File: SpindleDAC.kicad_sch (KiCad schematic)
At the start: 18 parts, among them J25 Spindle Out, Q1 BC847, U17 LTV-247, U18 TL431A

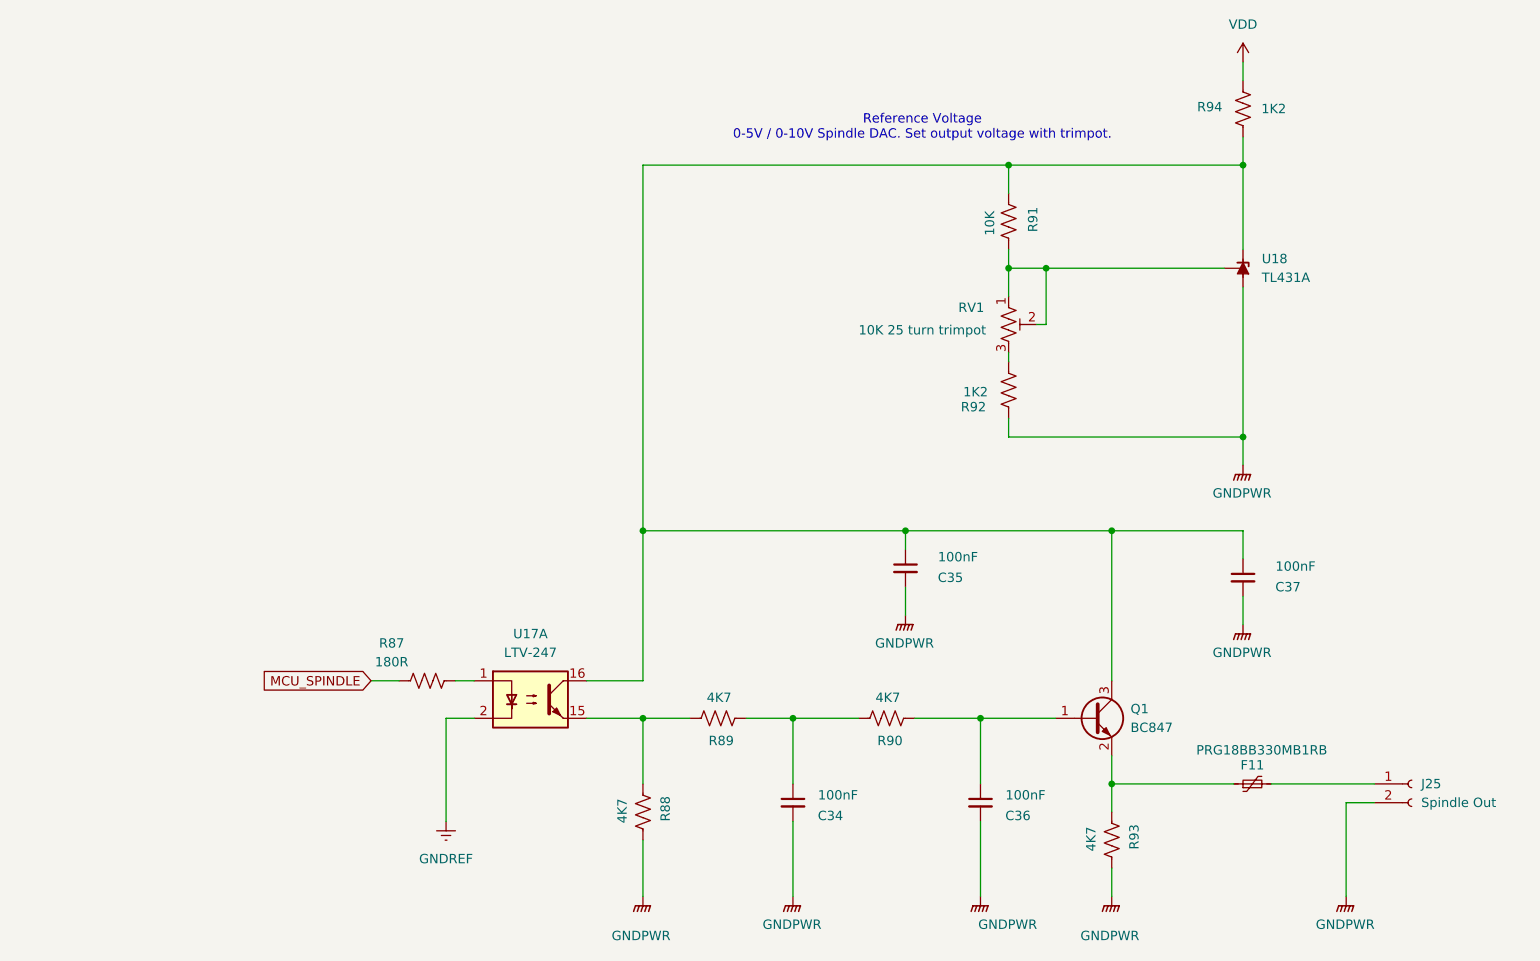
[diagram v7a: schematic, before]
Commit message: Switched terminal footprints over to a finer pitch. Corrected an issue with component reference values preventing proper use of multi channel rule areas. Component references for 4 channel optos are more straightforward as a result
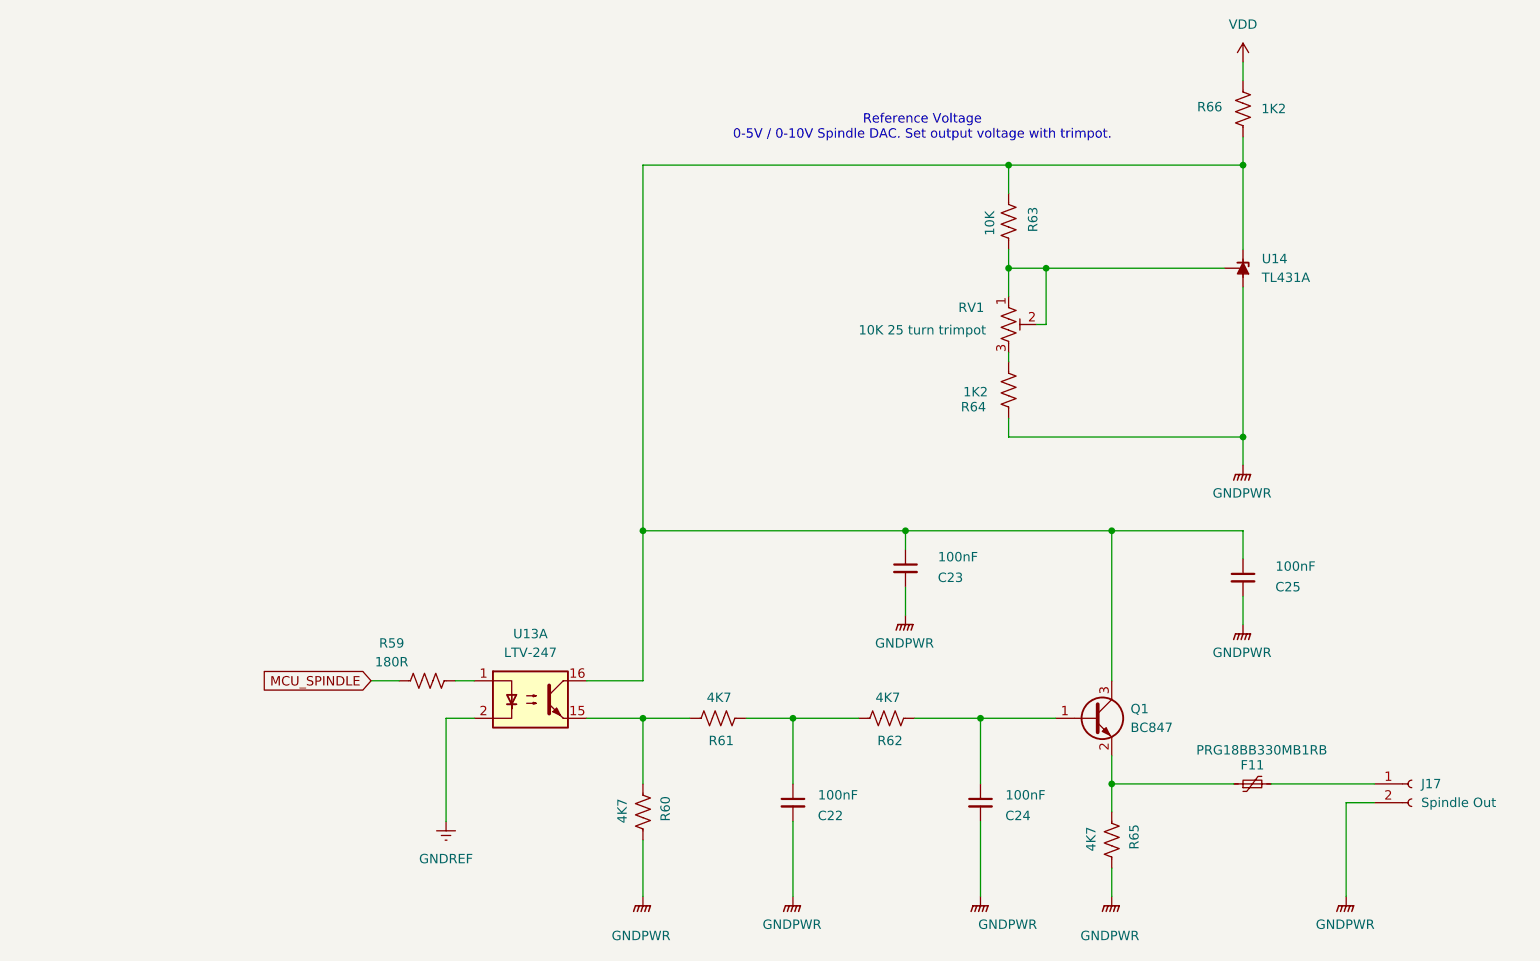
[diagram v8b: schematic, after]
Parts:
- removed U17: LTV-247, Package_SO:SOP-16_4.4x10.4mm_P1.27mm, symbol Isolator:LTV-247
- added U13: LTV-247, Package_SO:SOP-16_4.4x10.4mm_P1.27mm, symbol Isolator:LTV-247
- J17: renamed from J25; footprint EBWA_02_A:ADAMTECH_EBWA-02-A -> 691412120002B:691412120002B
- renumbered C34 to C22, C35 to C23, C36 to C24, C37 to C25, R87 to R59, R88 to R60, R89 to R61, R90 to R62, R91 to R63, R92 to R64, R93 to R65, R94 to R66, U18 to U14
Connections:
- net GNDREF: now also U13.2
- net at R60.1, R61.2: now also U13.15
- net at C23.1, C25.1, Q1.3 (C)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: now also U13.16
- net at R59.2: now also U13.1
